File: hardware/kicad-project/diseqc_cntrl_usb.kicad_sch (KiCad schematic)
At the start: 6 parts, among them J6 USB4110-GF-A, U1 FT230XS

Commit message: Add fiducials
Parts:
- renumbered C28 to C32, C29 to C33, R15 to R18, R16 to R19
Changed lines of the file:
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@@
 		(dnp no)
 		(fields_autoplaced yes)
-		(property "Reference" "#PWR049"
+		(property "Reference" "#PWR051"
 			(at 26.67 60.96 0)
 			(hide yes)
@@
 			(project "diseqc_cntrl"
 				(path "/82a905d8-f1d7-4995-9c16-94cf3cdcaad9/65fcf1a0-d0f2-4bf0-9977-67dd9f84afa5/e5108393-1145-4ace-bd05-28ed9bbcb2b1"
-					(reference "#PWR049")
+					(reference "#PWR051")
 					(unit 1)
 				)
@@
 		(in_pos_files yes)
 		(dnp no)
-		(property "Reference" "#PWR050"
+		(property "Reference" "#PWR052"
 			(at 80.01 92.71 0)
 			(hide yes)
@@
 			(project "diseqc_cntrl"
 				(path "/82a905d8-f1d7-4995-9c16-94cf3cdcaad9/65fcf1a0-d0f2-4bf0-9977-67dd9f84afa5/e5108393-1145-4ace-bd05-28ed9bbcb2b1"
-					(reference "#PWR050")
+					(reference "#PWR052")
 					(unit 1)
 				)
@@
 		(in_pos_files yes)
 		(dnp no)
-		(property "Reference" "R16"
+		(property "Reference" "R19"
 			(at 107.696 75.438 90)
 			(show_name no)
@@
 				(font
 					(size 1.27 1.27)
+				)
+			)
+		)
+		(property "VoltageRequirement" ""
+			(at 105.41 72.39 90)
+			(hide yes)
+			(show_name no)
+			(do_not_autoplace no)
+			(effects
+				(font
+					(size 0.762 0.762)
 				)
 			)
@@
 			(project "diseqc_cntrl"
 				(path "/82a905d8-f1d7-4995-9c16-94cf3cdcaad9/65fcf1a0-d0f2-4bf0-9977-67dd9f84afa5/e5108393-1145-4ace-bd05-28ed9bbcb2b1"
-					(reference "R16")
+					(reference "R19")
 					(unit 1)
 				)
@@
 		(dnp no)
 		(fields_autoplaced yes)
-		(property "Reference" "C28"
+		(property "Reference" "C32"
 			(at 83.82 78.7399 0)
 			(show_name no)
@@
 				(font
 					(size 1.27 1.27)
+				)
+			)
+		)
+		(property "VoltageRequirement" ""
+			(at 80.01 80.01 0)
+			(hide yes)
+			(show_name no)
+			(do_not_autoplace no)
+			(effects
+				(font
+					(size 0.762 0.762)
 				)
 			)
@@
 			(project "diseqc_cntrl"
 				(path "/82a905d8-f1d7-4995-9c16-94cf3cdcaad9/65fcf1a0-d0f2-4bf0-9977-67dd9f84afa5/e5108393-1145-4ace-bd05-28ed9bbcb2b1"
-					(reference "C28")
+					(reference "C32")
 					(unit 1)
 				)
@@
 		(dnp no)
 		(fields_autoplaced yes)
-		(property "Reference" "C29"
+		(property "Reference" "C33"
 			(at 144.78 77.4699 0)
 			(show_name no)
@@
 				(font
 					(size 1.27 1.27)
+				)
+			)
+		)
+		(property "VoltageRequirement" ""
+			(at 140.97 78.74 0)
+			(hide yes)
+			(show_name no)
+			(do_not_autoplace no)
+			(effects
+				(font
+					(size 0.762 0.762)
 				)
 			)
@@
 			(project "diseqc_cntrl"
 				(path "/82a905d8-f1d7-4995-9c16-94cf3cdcaad9/65fcf1a0-d0f2-4bf0-9977-67dd9f84afa5/e5108393-1145-4ace-bd05-28ed9bbcb2b1"
-					(reference "C29")
+					(reference "C33")
 					(unit 1)
 				)
@@
 			)
 		)
+		(property "VoltageRequirement" ""
+			(at 40.64 44.45 0)
+			(hide yes)
+			(show_name no)
+			(do_not_autoplace no)
+			(effects
+				(font
+					(size 0.762 0.762)
+				)
+			)
+		)
 		(pin "8"
 		)
@@
 		(in_pos_files yes)
 		(dnp no)
-		(property "Reference" "R15"
+		(property "Reference" "R18"
 			(at 99.568 75.946 90)
 			(show_name no)
@@
 				(font
 					(size 1.27 1.27)
+				)
+			)
+		)
+		(property "VoltageRequirement" ""
+			(at 101.6 72.39 90)
+			(hide yes)
+			(show_name no)
+			(do_not_autoplace no)
+			(effects
+				(font
+					(size 0.762 0.762)
 				)
 			)
@@
 			(project "diseqc_cntrl"
 				(path "/82a905d8-f1d7-4995-9c16-94cf3cdcaad9/65fcf1a0-d0f2-4bf0-9977-67dd9f84afa5/e5108393-1145-4ace-bd05-28ed9bbcb2b1"
-					(reference "R15")
+					(reference "R18")
 					(unit 1)
 				)
@@
 				)
 			)
+		)
+		(property "VoltageRequirement" ""
+			(at 137.16 64.77 0)
+			(hide yes)
+			(show_name no)
+			(do_not_autoplace no)
+			(effects
+				(font
+					(size 0.762 0.762)
+				)
+			)

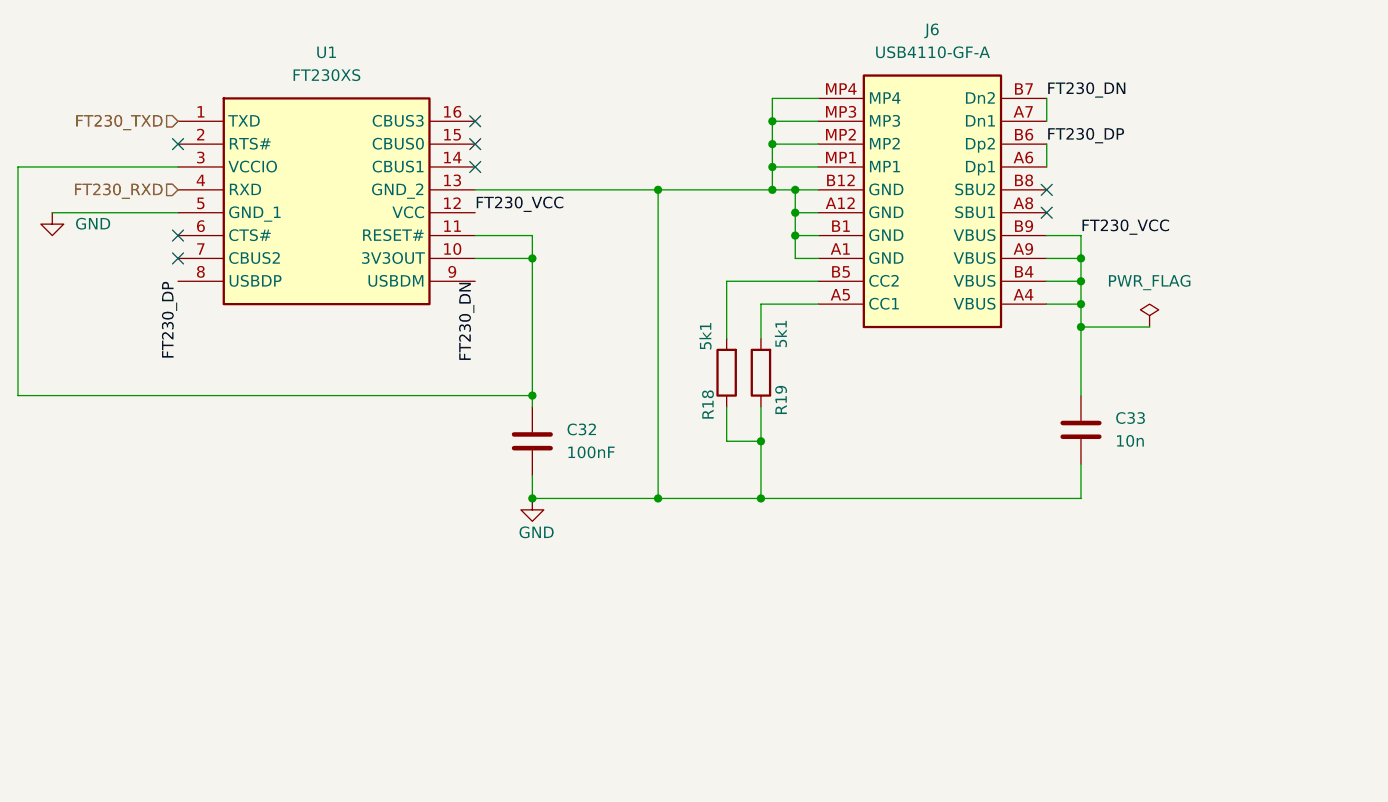
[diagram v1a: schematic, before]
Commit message: Upgraded power supplies
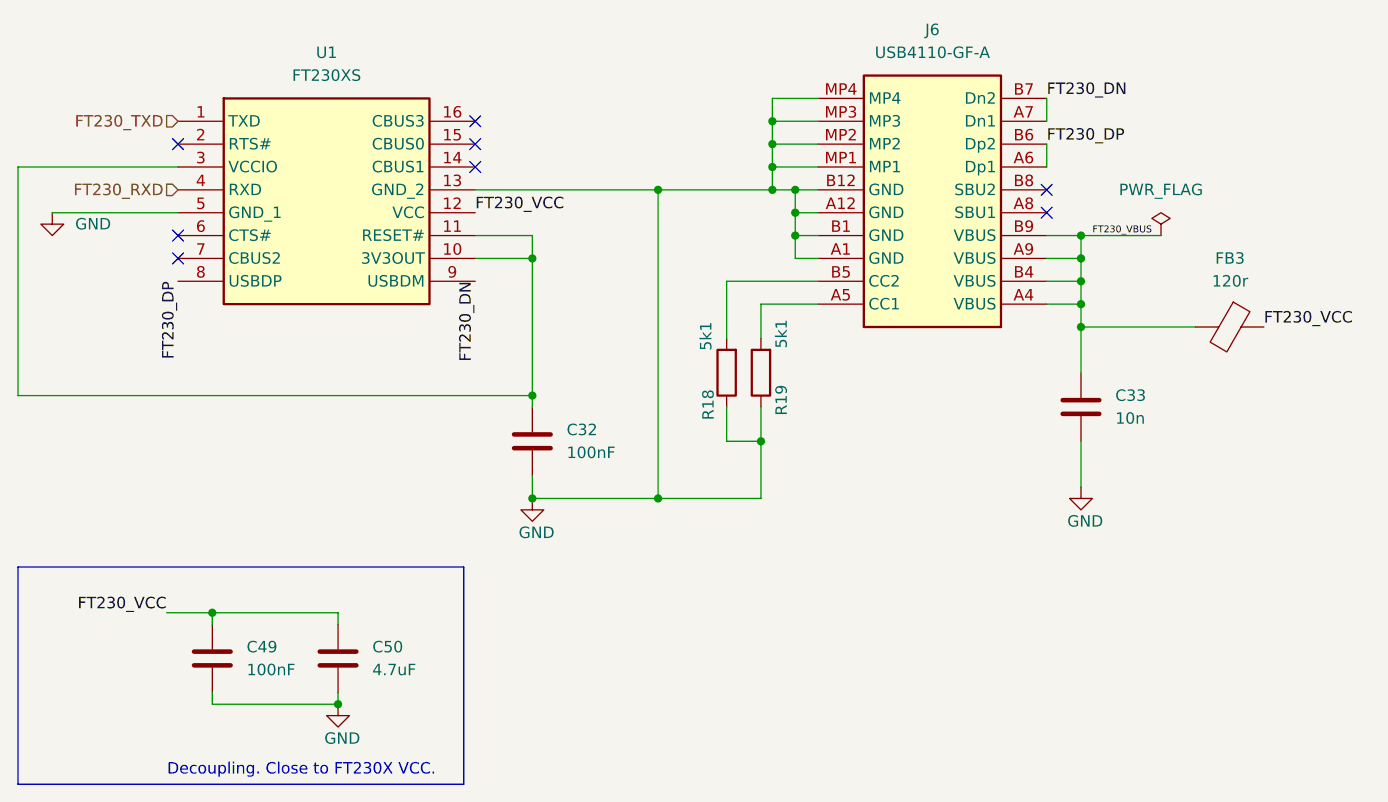
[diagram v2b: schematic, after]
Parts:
- added C49: 100nF, Capacitor_SMD:C_0603_1608Metric, symbol #InvenTree:C_100n_0603
- added C50: 4.7uF, Capacitor_SMD:C_0805_2012Metric, symbol #InvenTree:C_4u7_0805
- added FB3: 120r, Inductor_SMD:L_0603_1608Metric, symbol #InvenTree:FB_120r_0603
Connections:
- net FT230_VCC: now also C49.1, C50.2, FB3.1; no longer C33.1, J6.A4 (VBUS), J6.A9 (VBUS), J6.B4 (VBUS), J6.B9 (VBUS)
- net GND: now also C49.2, C50.1
- new net FT230_VBUS: C33.1, FB3.2, J6.A4 (VBUS), J6.A9 (VBUS), J6.B4 (VBUS), J6.B9 (VBUS)
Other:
- note added: "Decoupling. Close to FT230X VCC."
- moved on the sheet: C33
